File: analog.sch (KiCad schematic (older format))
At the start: 0 parts

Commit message: Began analog and digital schematic
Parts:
- added C?: C, symbol C
- added J?: Conn_02x17_Odd_Even, symbol Conn_02x17_Odd_Even
- added R? (x2): 4k99, symbol R
- added U? (x4): TL084, symbol TL084
- added U?: 4051, symbol 4051
- added U?: 74LS374, symbol 74LS374
- added U? (x2): TL072, symbol TL072
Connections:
- new net: J?.5 (Pin_5), R?.1
- new net: C?.1, R?.1, R?.2, U?.13 (X0)
- new net: U?.10 (B), U?.15 (O5)
- new net: U?.11 (A), U?.19 (O7)
- new net: U?.3 (X), U?.5 (+)
- new net: U?.16 (O6), U?.9 (C)
- new net: U?.6 (-), U?.7
- new net AMP1-OUT1: J?.25 (Pin_25)
- new net AMP1-OUT2: J?.23 (Pin_23)
- new net AMP1-OUT3: J?.21 (Pin_21)
- new net AMP1-OUT4: J?.19 (Pin_19)
- new net AMP2-OUT1: J?.33 (Pin_33)
- new net AMP2-OUT2: J?.31 (Pin_31)
- new net AMP2-OUT3: J?.29 (Pin_29)
- new net AMP2-OUT4: J?.27 (Pin_27)
- new net GND: C?.2, J?.1 (Pin_1), J?.2 (Pin_2), R?.2, U?.10 (GND)
- new net VCC: U?.20 (VCC)
- new net VDD: U?.16 (VDD)
- new net VSS: U?.8 (VSS)
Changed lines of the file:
@@
 $Descr A4 11693 8268
 encoding utf-8
-Sheet 1 3
+Sheet 1 1
 Title ""
 Date ""
@@
 Comment4 ""
 $EndDescr
+$Comp
+L Conn_02x17_Odd_Even J?
+U 1 1 5B427120
+P 6000 3550
+F 0 "J?" H 6050 4450 50  0000 C CNN
+F 1 "Conn_02x17_Odd_Even" H 6050 2650 50  0000 C CNN
+F 2 "" H 6000 3550 50  0001 C CNN
+F 3 "" H 6000 3550 50  0001 C CNN
+	1    6000 3550
+	1    0    0    -1
+$EndComp
+Wire Wire Line
+	6300 2750 6300 4750
+$Comp
+L GND #PWR?
+U 1 1 5B4271EF
+P 6300 4750
+F 0 "#PWR?" H 6300 4500 50  0001 C CNN
+F 1 "GND" H 6300 4600 50  0000 C CNN
+F 2 "" H 6300 4750 50  0001 C CNN
+F 3 "" H 6300 4750 50  0001 C CNN
+	1    6300 4750
+	1    0    0    -1
+$EndComp
+Wire Wire Line
+	5800 2750 5400 2750
+$Comp
+L GND #PWR?
+U 1 1 5B427286
+P 5400 2750
+F 0 "#PWR?" H 5400 2500 50  0001 C CNN
+F 1 "GND" H 5400 2600 50  0000 C CNN
+F 2 "" H 5400 2750 50  0001 C CNN
+F 3 "" H 5400 2750 50  0001 C CNN
+	1    5400 2750
+	1    0    0    -1
+$EndComp
+$Comp
+L TL084 U?
+U 1 1 5B427317
+P 7950 3550
+F 0 "U?" H 7950 3750 50  0000 L CNN
+F 1 "TL084" H 7950 3350 50  0000 L CNN
+F 2 "" H 7900 3650 50  0001 C CNN
+F 3 "" H 8000 3750 50  0001 C CNN
+	1    7950 3550
+	1    0    0    -1
+$EndComp
+$Comp
+L TL084 U?
+U 2 1 5B427384
+P 7950 4300
+F 0 "U?" H 7950 4500 50  0000 L CNN
+F 1 "TL084" H 7950 4100 50  0000 L CNN
+F 2 "" H 7900 4400 50  0001 C CNN
+F 3 "" H 8000 4500 50  0001 C CNN
+	2    7950 4300
+	1    0    0    -1
+$EndComp
+$Comp
+L TL084 U?
+U 3 1 5B4273DB
+P 7950 5050
+F 0 "U?" H 7950 5250 50  0000 L CNN
+F 1 "TL084" H 7950 4850 50  0000 L CNN
+F 2 "" H 7900 5150 50  0001 C CNN
+F 3 "" H 8000 5250 50  0001 C CNN
+	3    7950 5050
+	1    0    0    -1
+$EndComp
+$Comp
+L TL084 U?
+U 4 1 5B42742E
+P 7950 5800
+F 0 "U?" H 7950 6000 50  0000 L CNN
+F 1 "TL084" H 7950 5600 50  0000 L CNN
+F 2 "" H 7900 5900 50  0001 C CNN
+F 3 "" H 8000 6000 50  0001 C CNN
+	4    7950 5800
+	1    0    0    -1
+$EndComp
+Wire Wire Line
+	5800 4350 5150 4350
+Wire Wire Line
+	5800 4250 5150 4250
+Wire Wire Line
+	5800 4150 5150 4150
+Wire Wire Line
+	5800 4050 5150 4050
+Wire Wire Line
+	5800 3950 5150 3950
+Wire Wire Line
+	5800 3850 5150 3850
+Wire Wire Line
+	5800 3750 5150 3750
+Wire Wire Line
+	5800 3650 5150 3650
+Text Label 5150 3650 0    60   ~ 0
+AMP1-OUT4
+Text Label 5150 3750 0    60   ~ 0
+AMP1-OUT3
+Text Label 5150 3850 0    60   ~ 0
+AMP1-OUT2
+Text Label 5150 3950 0    60   ~ 0
+AMP1-OUT1
+Text Label 5150 4050 0    60   ~ 0
+AMP2-OUT4
+Text Label 5150 4150 0    60   ~ 0
+AMP2-OUT3
+Text Label 5150 4250 0    60   ~ 0
+AMP2-OUT2
+Text Label 5150 4350 0    60   ~ 0
+AMP2-OUT1
+Wire Wire Line
+	5800 2950 4550 2950
+$Comp
+L R R?
+U 1 1 5B4292DE
+P 4550 3100
+F 0 "R?" V 4630 3100 50  0000 C CNN
+F 1 "4k99" V 4550 3100 50  0000 C CNN
+F 2 "" V 4480 3100 50  0001 C CNN
+F 3 "" H 4550 3100 50  0001 C CNN
+	1    4550 3100
+	1    0    0    -1
+$EndComp
+$Comp
+L R R?
+U 1 1 5B42930D
+P 4550 3400
+F 0 "R?" V 4630 3400 50  0000 C CNN
+F 1 "4k99" V 4550 3400 50  0000 C CNN
+F 2 "" V 4480 3400 50  0001 C CNN
+F 3 "" H 4550 3400 50  0001 C CNN
+	1    4550 3400
+	1    0    0    -1
+$EndComp
+$Comp
+L GND #PWR?
+U 1 1 5B429546
+P 4550 3550
+F 0 "#PWR?" H 4550 3300 50  0001 C CNN
+F 1 "GND" H 4550 3400 50  0000 C CNN
+F 2 "" H 4550 3550 50  0001 C CNN
+F 3 "" H 4550 3550 50  0001 C CNN
+	1    4550 3550
+	1    0    0    -1
+$EndComp
+$Comp
+L C C?
+U 1 1 5B429645
+P 4050 3400
+F 0 "C?" H 4075 3500 50  0000 L CNN
+F 1 "C" H 4075 3300 50  0000 L CNN
+F 2 "" H 4088 3250 50  0001 C CNN
+F 3 "" H 4050 3400 50  0001 C CNN
+	1    4050 3400
+	1    0    0    -1
+$EndComp
+Wire Wire Line
+	4550 3550 4050 3550
+Wire Wire Line
+	2250 3250 4550 3250
+$Comp
+L 4051 U?
+U 1 1 5B429874
+P 3100 4400
+F 0 "U?" H 3200 4400 50  0000 C CNN
+F 1 "4051" H 3200 4200 50  0000 C CNN
+F 2 "" H 3100 4400 60  0001 C CNN
+F 3 "" H 3100 4400 60  0001 C CNN
+	1    3100 4400
+	1    0    0    -1
+$EndComp
+Wire Wire Line
+	2250 3250 2250 3800
+Wire Wire Line
+	2250 3800 2400 3800
+Connection ~ 4050 3250
+$Comp
+L 74LS374 U?
+U 1 1 5B42A60B
+P 1200 5050
+F 0 "U?" H 1200 5050 50  0000 C CNN
+F 1 "74LS374" H 1250 4700 50  0000 C CNN
+F 2 "" H 1200 5050 50  0001 C CNN
+F 3 "" H 1200 5050 50  0001 C CNN
+	1    1200 5050
+	1    0    0    -1
+$EndComp
+Wire Wire Line
+	1900 5250 2400 4800
+Wire Wire Line
+	1900 5150 2400 5000
+Wire Wire Line
+	1900 5050 2400 4900
+$Comp
+L TL072 U?
+U 1 1 5B42BBBA
+P 4600 4750
+F 0 "U?" H 4600 4950 50  0000 L CNN
+F 1 "TL072" H 4600 4550 50  0000 L CNN
+F 2 "" H 4600 4750 50  0001 C CNN
+F 3 "" H 4600 4750 50  0001 C CNN
+	1    4600 4750
+	1    0    0    -1
+$EndComp
+$Comp
+L TL072 U?
+U 2 1 5B42BC18
+P 4600 5550
+F 0 "U?" H 4600 5750 50  0000 L CNN
+F 1 "TL072" H 4600 5350 50  0000 L CNN
+F 2 "" H 4600 5550 50  0001 C CNN
+F 3 "" H 4600 5550 50  0001 C CNN
+	2    4600 5550
+	1    0    0    -1
+$EndComp
+Wire Wire Line
+	4300 5450 3800 3800
+Wire Wire Line
+	4900 5550 4900 5950
+Wire Wire Line
+	4900 5950 4300 5950
+Wire Wire Line
+	4300 5950 4300 5650
 $EndSCHEMATC

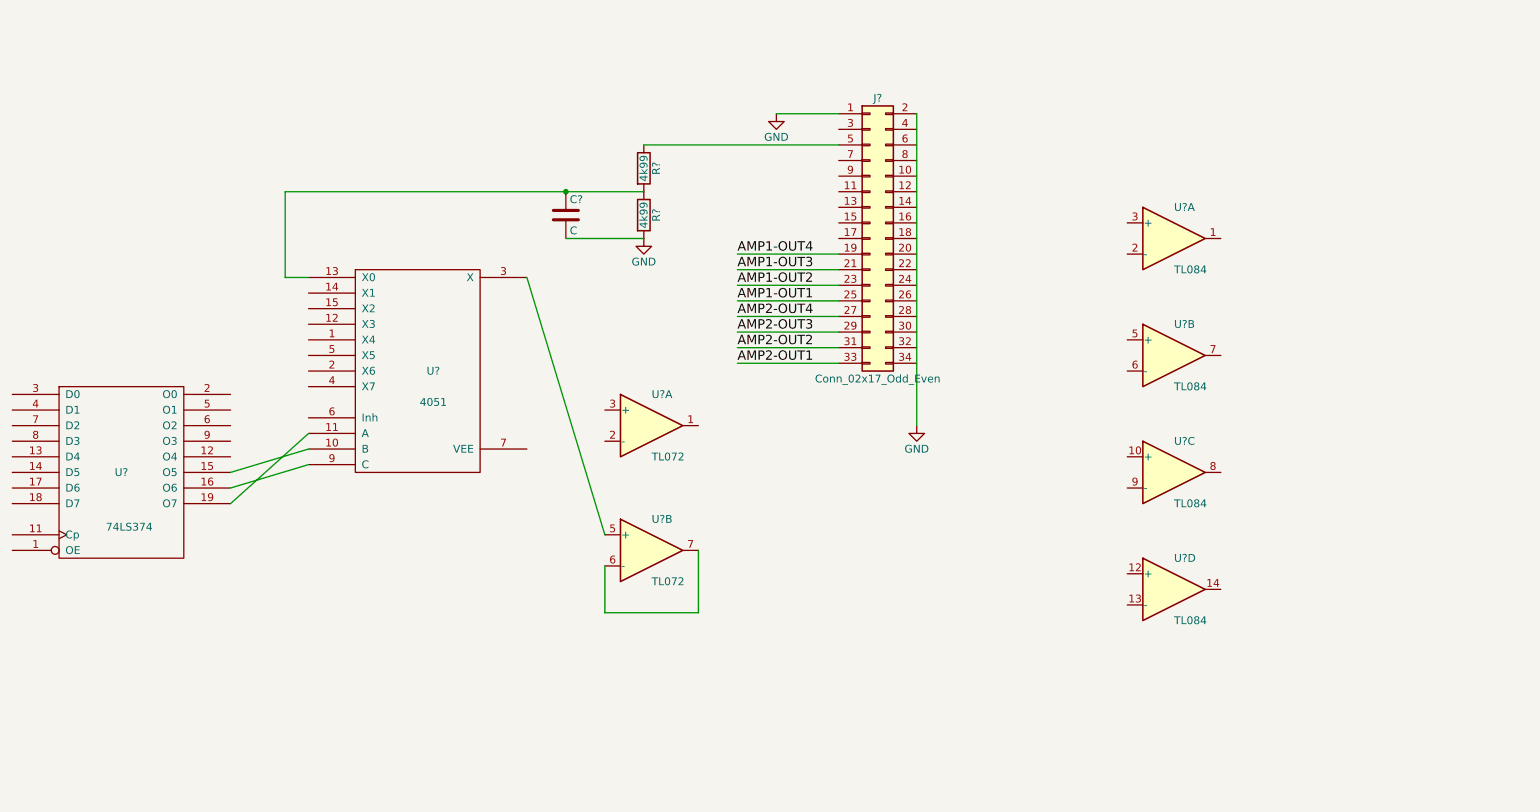
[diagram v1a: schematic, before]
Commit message: Fixed schematic to work with KiCad 5
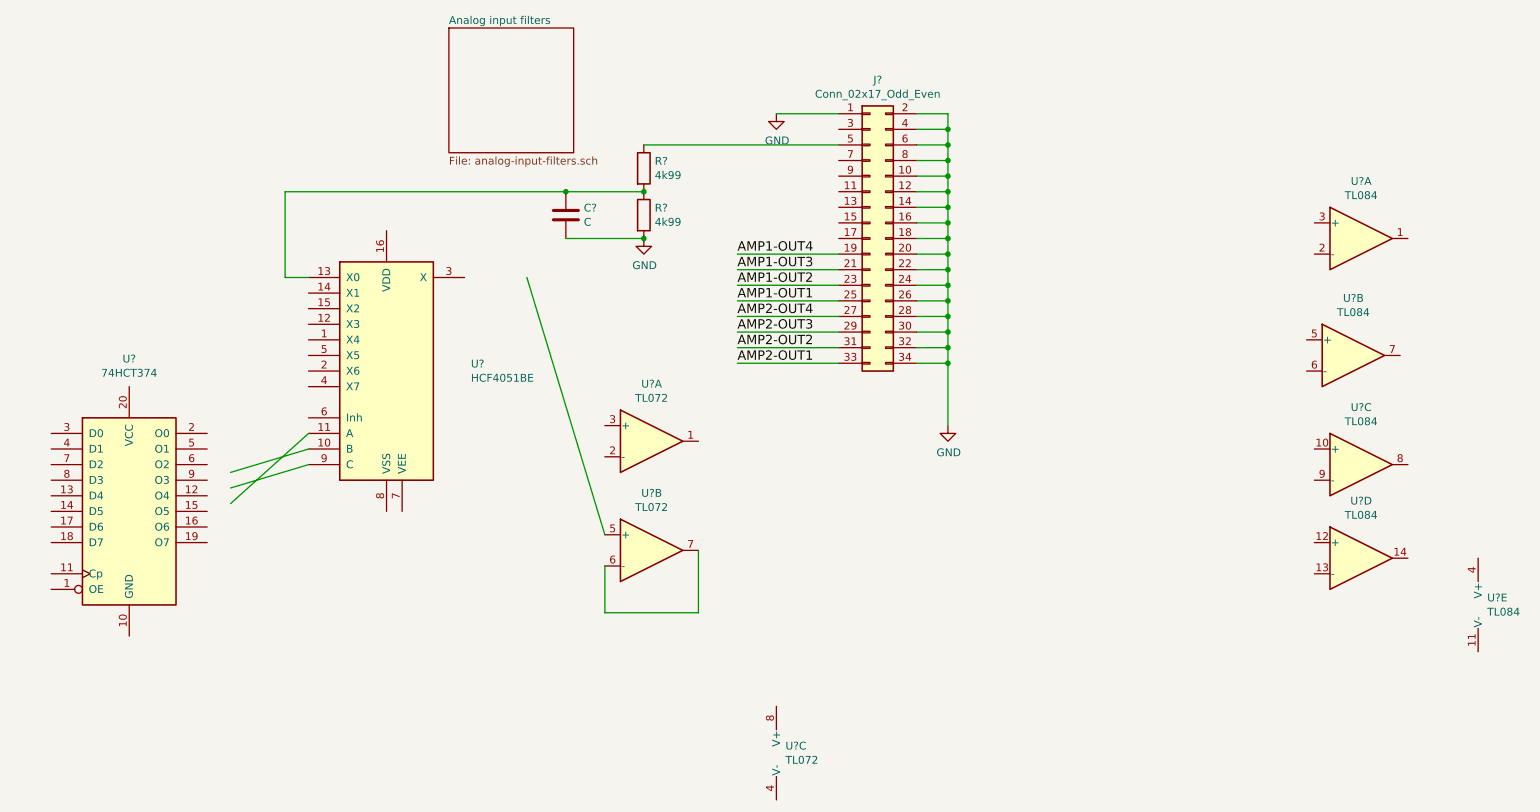
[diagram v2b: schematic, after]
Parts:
- removed C?: C, symbol C
- removed J?: Conn_02x17_Odd_Even, symbol Conn_02x17_Odd_Even
- removed R? (x2): 4k99, symbol R
- removed U? (x4): TL084, symbol TL084
- removed U?: 4051, symbol 4051
- removed U?: 74LS374, symbol 74LS374
- removed U? (x2): TL072, symbol TL072
- added C?: C, symbol Device:C
- added J?: Conn_02x17_Odd_Even, symbol Connector_Generic:Conn_02x17_Odd_Even
- added R? (x2): 4k99, symbol Device:R
- added U? (x3): TL072, symbol Amplifier_Operational:TL072
- added U? (x5): TL084, symbol Amplifier_Operational:TL084
- added U?: HCF4051BE, symbol 4xxx:4051
- added U?: 74HCT374, symbol 74xx:74LS374
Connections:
- wire segments 22 -> 56
